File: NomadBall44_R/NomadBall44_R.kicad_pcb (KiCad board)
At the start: 2 copper layers, 147.4 x 96.5 mm, 56 parts, among them SW1 SW_Push, SW10 SW_Push, SW11 SW_Push, SW12 SW_Push, SW13 SW_Push, SW14 SW_Push, SW15 SW_Push, SW16 SW_Push, SW17 SW_Push, SW18 SW_Push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

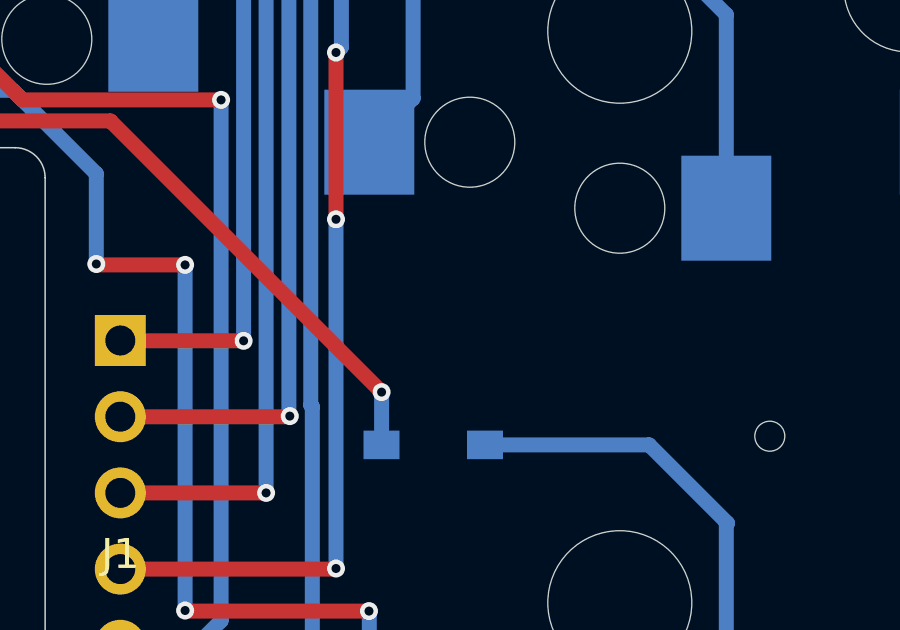
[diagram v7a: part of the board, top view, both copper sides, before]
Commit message: ネジ穴を一つ追加
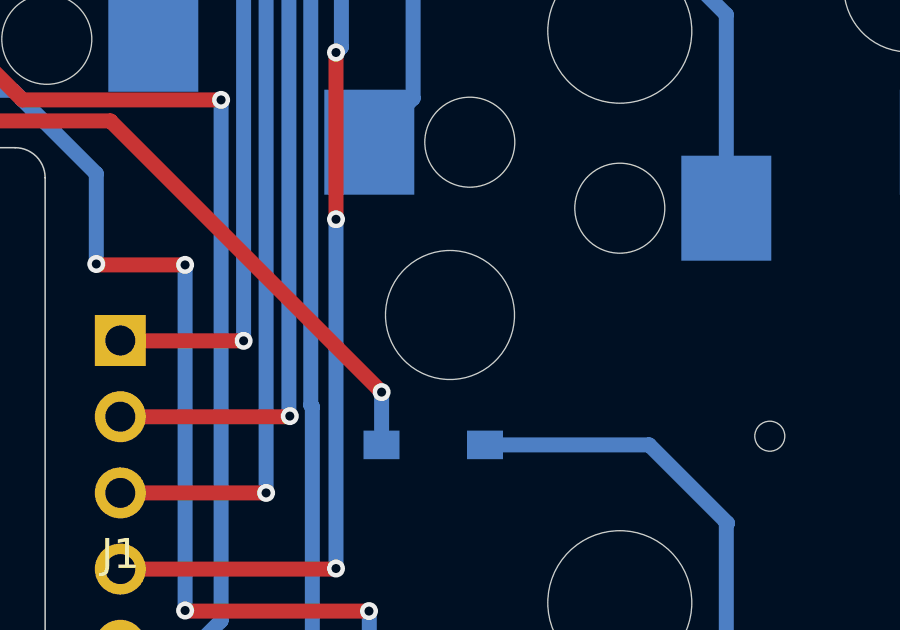
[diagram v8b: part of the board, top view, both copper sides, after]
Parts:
- added REF**: MountingHole_4.3mm_M4, MountingHole:MountingHole_4.3mm_M4, F.Cu at (186.3, 108.4)
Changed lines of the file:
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@@
+		(embedded_fonts no)
+	)
+	(footprint "MountingHole:MountingHole_4.3mm_M4"
+		(layer "F.Cu")
+		(at 186.26 108.44)
+		(descr "Mounting Hole 4.3mm, M4, no annular, generated by kicad-footprint-generator mountinghole.py")
+		(tags "mountinghole M4")
+		(property "Reference" "REF**"
+			(at 0 -5.25 0)
+			(layer "F.SilkS")
+			(hide yes)
+			(effects
+				(font
+					(size 1 1)
+					(thickness 0.15)
+				)
+			)
+		)
+		(property "Value" "MountingHole_4.3mm_M4"
+			(at 0 5.25 0)
+			(layer "F.Fab")
+			(effects
+				(font
+					(size 1 1)
+					(thickness 0.15)
+				)
+			)
+		)
+		(property "Datasheet" ""
+			(at 0 0 0)
+			(layer "F.Fab")
+			(hide yes)
+			(effects
+				(font
+					(size 1.27 1.27)
+					(thickness 0.15)
+				)
+			)
+		)
+		(property "Description" ""
+			(at 0 0 0)
+			(layer "F.Fab")
+			(hide yes)
+			(effects
+				(font
+					(size 1.27 1.27)
+					(thickness 0.15)
+				)
+			)
+		)
+		(attr exclude_from_pos_files exclude_from_bom)
+		(fp_circle
+			(center 0 0)
+			(end 4.3 0)
+			(stroke
+				(width 0.15)
+				(type solid)
+			)
+			(fill no)
+			(layer "Cmts.User")
+		)
+		(fp_circle
+			(center 0 0)
+			(end 4.55 0)
+			(stroke
+				(width 0.05)
+				(type solid)
+			)
+			(fill no)
+			(layer "F.CrtYd")
+		)
+		(fp_text user "${REFERENCE}"
+			(at 0 0 0)
+			(layer "F.Fab")
+			(effects
+				(font
+					(size 1 1)
+					(thickness 0.15)
+				)
+			)
+		)
+		(pad "" np_thru_hole circle
+			(at 0 0)
+			(size 4.3 4.3)
+			(drill 4.3)
+			(layers "*.Cu" "*.Mask")
+		)
 		(embedded_fonts no)
 	)
